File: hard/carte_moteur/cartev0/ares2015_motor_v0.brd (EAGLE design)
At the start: 68.6 x 53.3 mm, 60 parts, among them CN1 1X4-CLEANBIG, IC1 TB6612FNG, J1 1X5, Q1 AOD417, U1 DRV8828PWP, U2 PCA9685

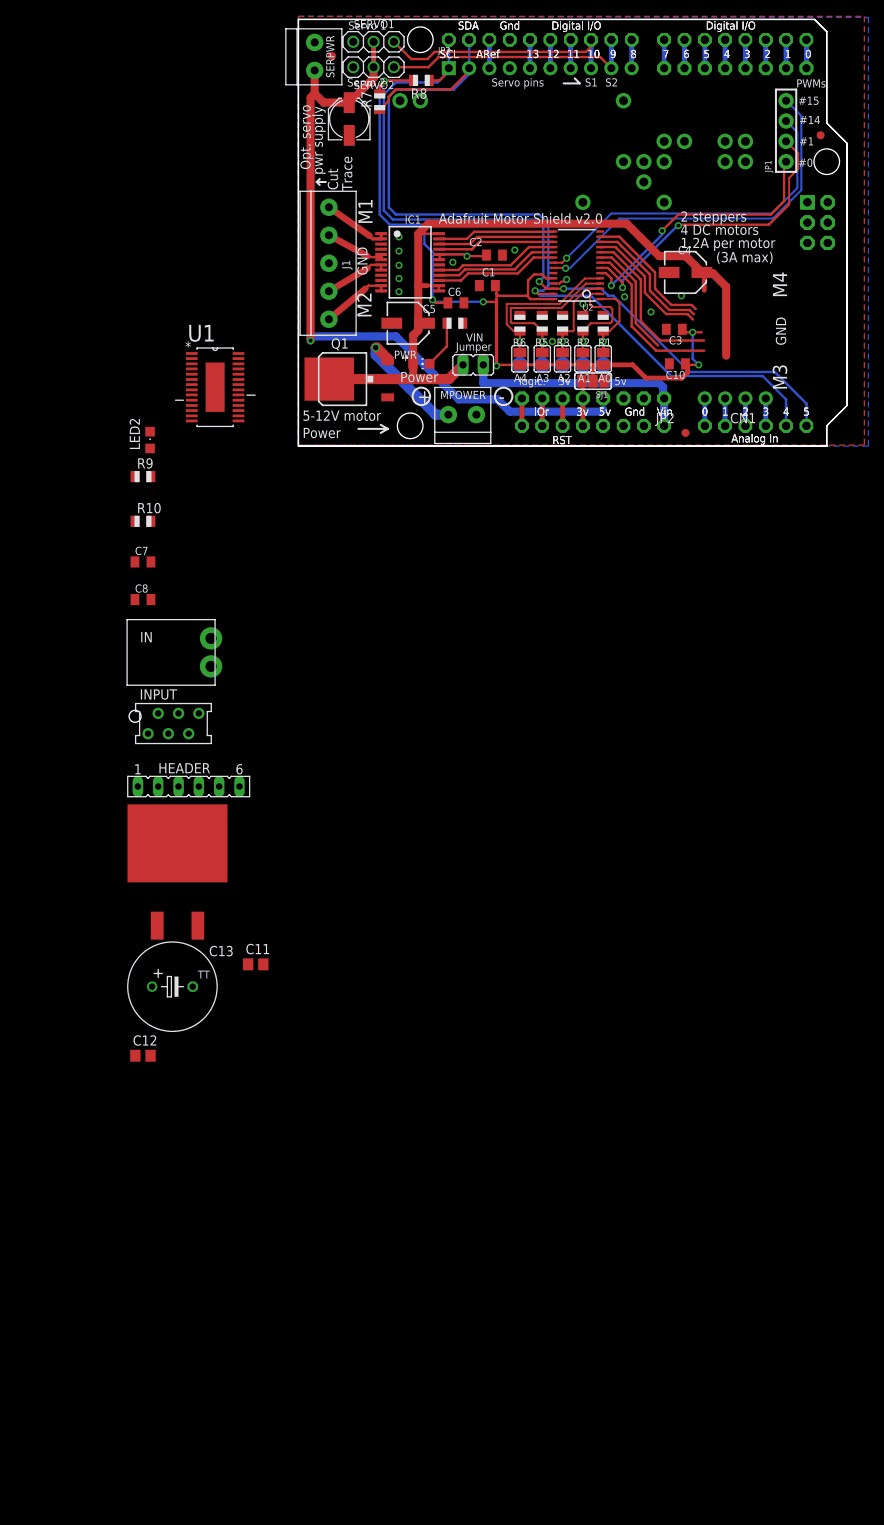
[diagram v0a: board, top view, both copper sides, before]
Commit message: maj schema carte moteur (80% de schema finit)
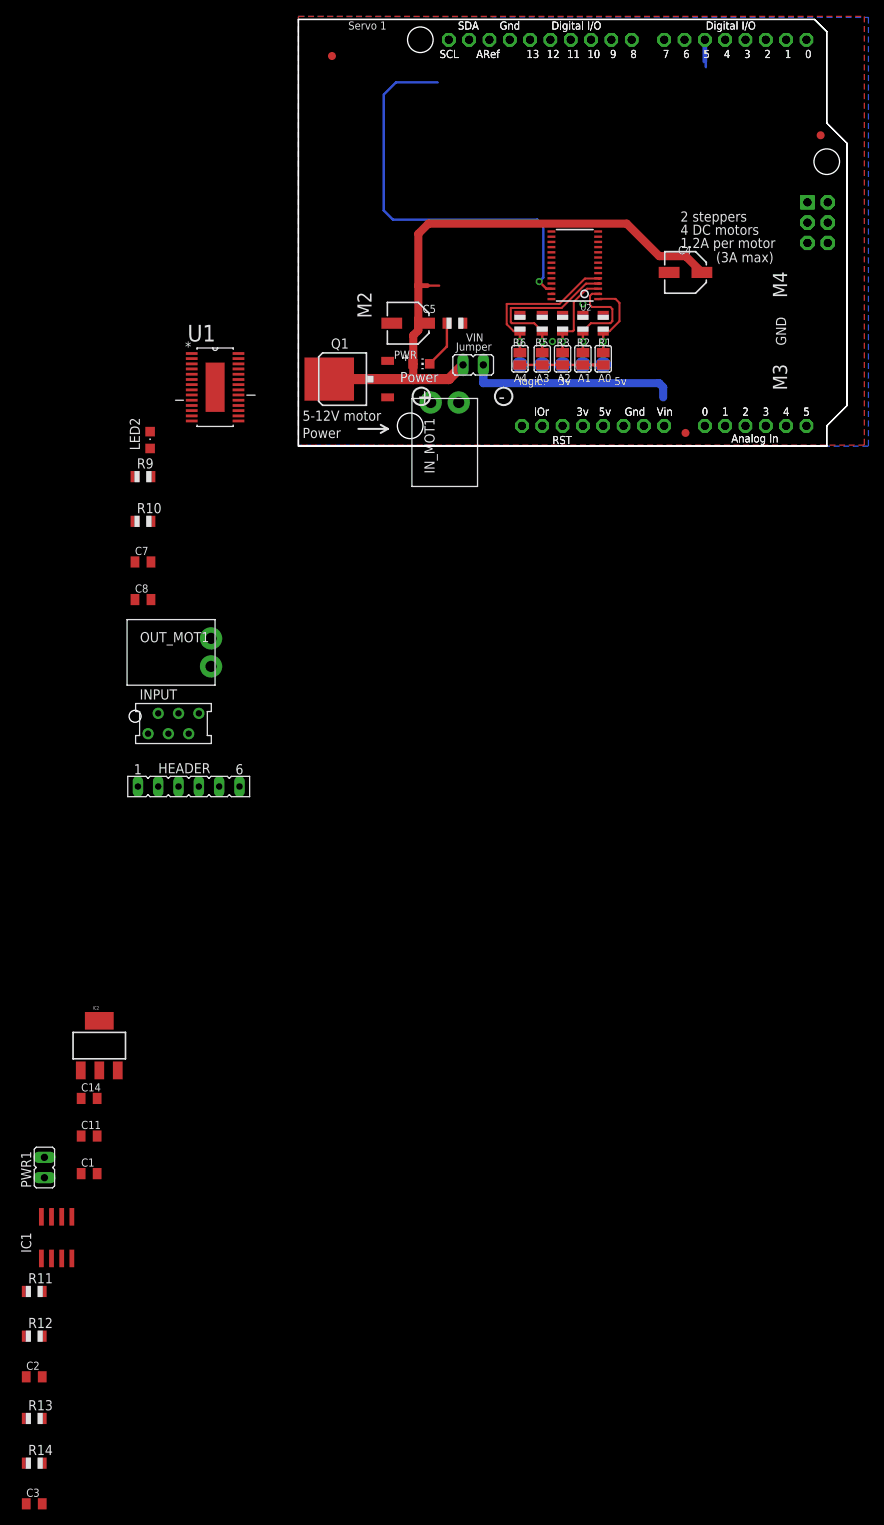
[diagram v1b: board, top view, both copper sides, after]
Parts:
- removed C10, C6: 10uF, adafruit:C0805K
- removed C12: 330nF, rcl:C0805
- removed C13: 2200u, rcl:TT5D11
- removed C9: 100uF, adafruit:PANASONIC_C
- removed CN1: 1X4-CLEANBIG, adafruit:1X04-CLEANBIG
- removed D0-7, JP2: (no value), adafruit:1X08-CLEANBIG
- removed J1: 1X5, adafruit:1X05-3.5MM
- removed JP1: (no value), microbuilder:1X04_ROUND_76
- removed JP3: (no value), microbuilder:1X10_ROUND70
- removed MPOWER, SERPWR: 1X2-3.5MM, adafruit:1X2-3.5MM
- removed R7, R8: 10K, adafruit:R0805
- removed SERVO1, SERVO2: (no value), adafruit:1X03
- removed SJ1: (no value), microbuilder:SOLDERJUMPER_2WAY_OPEN_NOPASTE
- removed U$6: L7805TO263, st-microelectronics:DPAK
- added C14: 0.1uF, adafruit:C0805K
- added IC2: (no value), SparkFun-PowerIC:SOT223
- added IN_MOT1: SL-3.5-2-90G, WEIDMULLER:SL-3.5-2-90G
- added PWR1: (no value), jumper:JP1
- added R11: 135k, adafruit:R0805
- added R12, R13, R14: 1.5k, adafruit:R0805
- C1: value 0.1uF -> 0.47uF
- C11: value 100nF -> 0.1uF; device rcl:C0805 -> adafruit:C0805K
- IC1: value TB6612FNG -> ISO7220A; device adafruit:SSOP24 -> texas:SO-08
- moved C3 167.2 mm to (-33.0, -132.2), turned to 0 degrees
- moved C2 151.6 mm to (-33.0, -116.3)
- moved IC1 129.7 mm to (-30.2, -98.9), turned to 0 degrees
- moved C1 121.7 mm to (-26.2, -90.9), turned to 0 degrees
- moved C11 29.9 mm to (-26.2, -86.2)
- moved U2 0.25 mm to (34.5, 22.6)
- renumbered IN to OUT_MOT1
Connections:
- removed net +3V3: JP2.5, SJ1.3, U$1.3V, U$5.3V
- removed net +5V: C11.2, C9.+, JP2.4, SERPWR.1, SERVO1.2, SERVO2.2, SJ1.1, U$1.5V_ICSP, U$5.5V_ICSP, U$6.3
- removed net GNDA: C11.1, C12.1, C13.-, OUT_MOT1.1, U$6.1
- removed net N$16: U1.5
- removed net N$33: U1.8
- removed net N$7: IC1.7, IC1.8, J1.2
- removed net PWM1A: JP3.9, SERVO2.3, U$1.D9, U$5.D9
- new net GND_CLEAN: C2.2, IC1.5, PWR1.2, U$1.GND@1, U$1.GND@2, U$5.GND@1, U$5.GND@2
- new net N$12: OUT_MOT1.2, U1.7, U1.8
- new net N$14: OUT_MOT1.1, U1.10, U1.5
- new net N$15: U$1.A5, U$5.A5
- new net N$17: U$1.A4, U$5.A4
- new net N$34: U$1.GND, U$5.GND
- new net SCL_CLEAN: IC1.6, R11.1, U$1.SCL, U$5.SCL
- new net SDA_CLEAN: IC1.7, R12.1, U$1.SDA, U$5.SDA
- new net VCC_CLEAN: C2.1, IC1.8, R11.2, R12.2, U$1.3V, U$5.3V
- net +12V: now also IC2.3; no longer C12.2, C13.+, IC1.13, IC1.14, IC1.24, OUT_MOT1.2, U$6.2
- net /RST: no longer JP2.6
- net GND: now also C11.2, C14.2, IC2.1, IN_MOT1.1, PWR1.1; no longer C10.2, C2.2, C6.2, C9.-, IC1.10, IC1.18, IC1.3, IC1.9, J1.3, JP2.2, JP2.3, JP3.4, MPOWER.1, SERPWR.2, SERVO1.1, SERVO2.1, U$1.GND, U$1.GND@1, U$1.GND@2, U$5.GND, U$5.GND@1, U$5.GND@2
- net N$1: no longer JP2.7
- net N$140: now also IN_MOT1.2; no longer MPOWER.2
- net N$18: now also IC1.2, R13.1; no longer U1.7
- net N$19: now also IC1.3, R14.1; no longer U1.10
- net N$2: no longer JP2.8
- net N$20: no longer CN1.4
- net N$21: no longer CN1.3
- net N$22: no longer CN1.2
- net N$23: no longer CN1.1
- net N$24: no longer D0-7.1
- net N$25: no longer D0-7.2
- net N$26: no longer D0-7.3
- net N$27: no longer D0-7.5
- net N$28: no longer D0-7.8
- net N$29: no longer JP3.10
- net N$30: no longer JP3.6
- net N$31: no longer JP3.5
- net N$32: no longer JP3.3
- net N$4: now also U$1.D9, U$5.D9; no longer IC1.1, IC1.2, J1.5
- net N$6: now also U1.21; no longer IC1.5, IC1.6, J1.4
- net N$9: now also U$1.5V_ICSP, U$5.5V_ICSP; no longer IC1.11, IC1.12, J1.1
- net PWM0: no longer JP1.1
- net PWM0A: no longer D0-7.7
- net PWM0B: no longer D0-7.6
- net PWM1: no longer JP1.2
- net PWM10: no longer IC1.21
- net PWM11: no longer IC1.17
- net PWM12: no longer IC1.16
- net PWM13: no longer IC1.15
- net PWM14: no longer JP1.3
- net PWM15: no longer JP1.4
- net PWM1B: no longer JP3.8, SERVO1.3
- net PWM2A: no longer JP3.7
- net PWM2B: no longer D0-7.4
- net PWM8: no longer IC1.23
- net PWM9: no longer IC1.22
- net SCL: no longer JP3.1, R8.1, U$1.A5, U$1.SCL, U$5.A5, U$5.SCL
- net SDA: no longer JP3.2, R7.1, U$1.A4, U$1.SDA, U$5.A4, U$5.SDA
- net V3POUT1: now also C1.1
- net VCC: now also C11.1, C14.1, IC1.1, IC2.2, IC2.4; no longer C1.1, C10.1, C2.1, C6.1, IC1.19, IC1.20, R7.2, R8.2, SJ1.2
- net VIN: no longer JP2.1
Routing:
- net VCC: track 131.6 -> 11.7 mm, vias 7 -> 0
- net SDA: track 116.4 -> 0.27 mm, vias 1 -> 0
- net +5V: track 90.4 -> 0.00 mm, vias 1 -> 0
- net SCL: track 101.5 -> 51.7 mm, vias 2 -> 1
- net PWM15: track 47.0 -> 0.00 mm, vias 1 -> 0
- net PWM14: track 43.3 -> 0.00 mm, vias 1 -> 0
- net PWM1: track 38.8 -> 0.00 mm, vias 2 -> 0
- net PWM0: track 33.9 -> 0.00 mm, vias 2 -> 0
- net PWM1A: track 31.8 -> 0.00 mm
- net PWM1B: track 30.6 -> 0.00 mm
- net PWM2: track 20.6 -> 0.00 mm
- net PWM4: track 20.6 -> 0.00 mm
- net +12V: track 96.8 -> 78.5 mm
- net PWM7: track 16.9 -> 0.00 mm
- net PWM6: track 16.7 -> 0.00 mm
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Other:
- board text removed: "#0"
- board text removed: "#1"
- board text removed: "#14"
- board text removed: "#15"
- board text removed: "Adafruit Motor Shield v2.0"
- board text removed: "Cut"
- board text removed: "M1"
- board text removed: "Opt. servo"
- board text removed: "PWMs"
- board text removed: "S1"
- board text removed: "S2"
- board text removed: "Servo 2"
- board text removed: "Servo pins"
- board text removed: "Trace"
- board text removed: "pwr supply"
